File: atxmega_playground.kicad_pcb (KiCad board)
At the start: 2 copper layers, 87 parts, among them CON1 AVR-PDI-6, IC1 ATXMEGA32A4U-A, P1 USB_OTG, P2 CONN_01X02, P3 CONN_01X02, P4 CONN_01X08, P5 CONN_01X03, P6 CONN_01X04, P7 CONN_01X04, Q1 PMOS, Q2 NMOS, Q3 NMOS, Q4 NMOS, U1 NCP346, U10 WS2812B, U11 WS2812B, U12 74HC595_F, U13 74HC595_F, U14 AT25SF041, U15 LM75BD, U16 HIH9131, U2 LM3940, U3 ADM3315E, U4 HI-3110, U5 INA139, U6 WS2812B, U7 SN65220, U8 WS2812B, Y1 16MHz

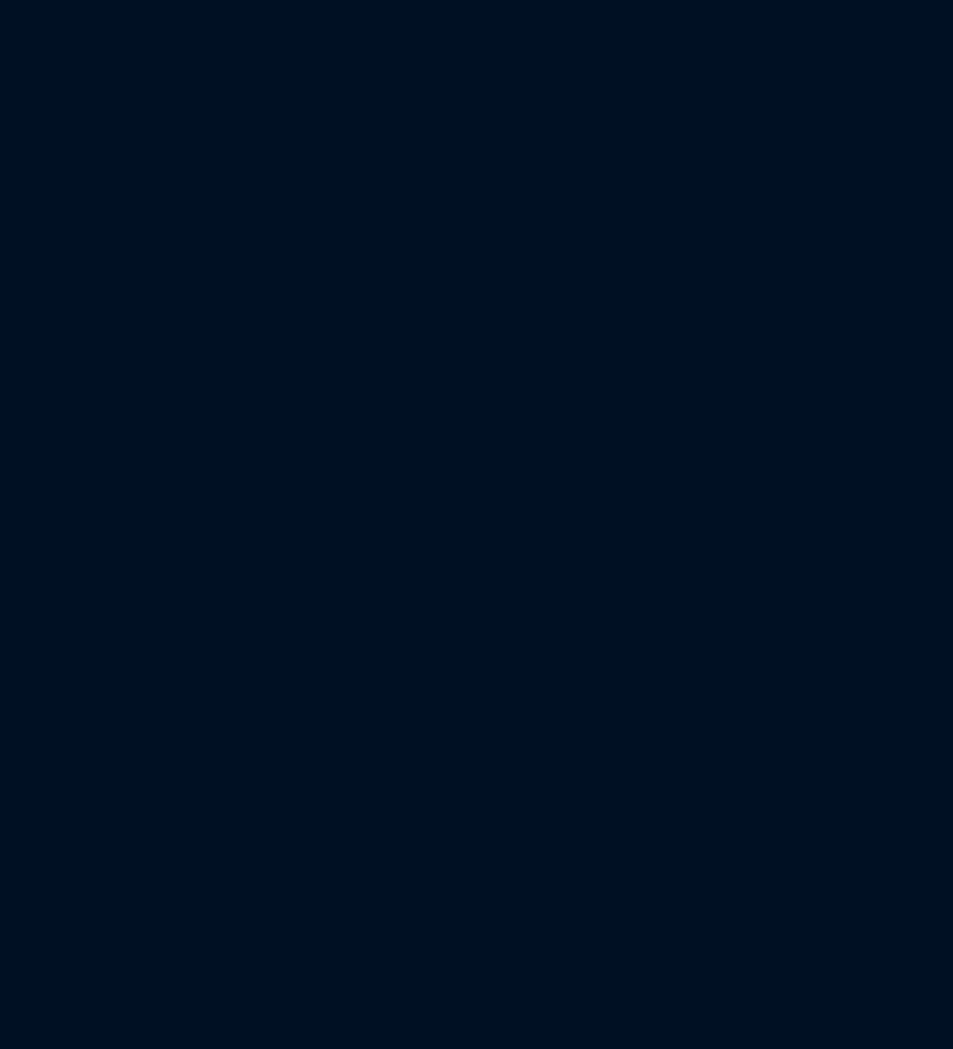
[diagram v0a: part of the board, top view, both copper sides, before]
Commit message: Add GPIO's ADC and 5V sensors, 7seg display footprint, and HIM's IMU's
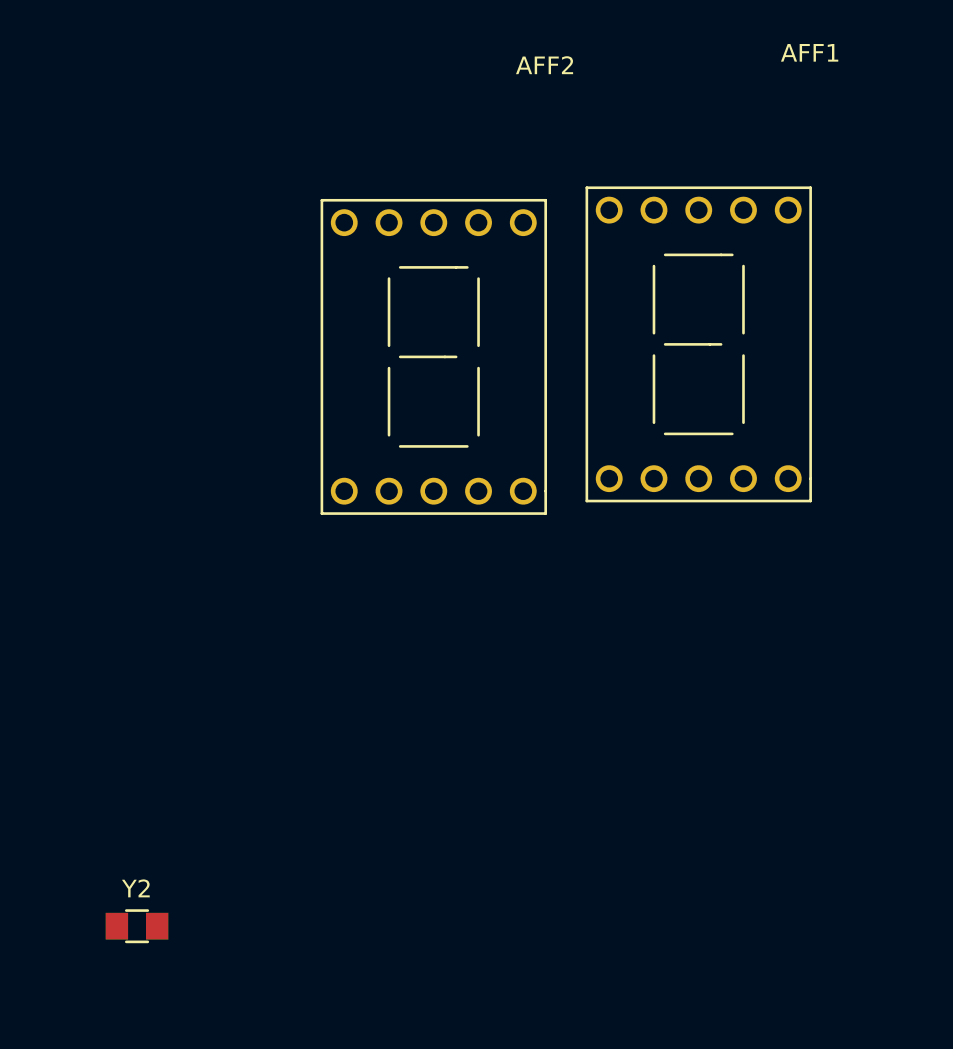
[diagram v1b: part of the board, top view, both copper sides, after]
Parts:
- added AFF1: 7SEGMENTS, atxmega:7seg_SC56-11SRWA, F.Cu at (201.0, 36.1)
- added AFF2: 7SEGMENTS, atxmega:7seg_SC56-11SRWA, F.Cu at (185.9, 36.8)
- added Y2: 32.768kHz, atxmega:R_0805, F.Cu at (174.2, 76.8)
- C15: value 0.1uF -> 10uF
- C16: value 0.22uF -> 0.1uF
- U15: value LM75BD -> REF195
- U16: value HIH9131 -> AD7708
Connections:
- net /ADC1 renamed /MC_ADC1
- net /ADC2 renamed /MC_ADC2
- net /ADC3 renamed /MC_ADC3
- net Net-(U16-Pad7) renamed /Vpressure
- C15 pad 1: Net-(C15-Pad1) -> +12V
- C16 pad 1: +3V3 -> +12V
- U15 pad 1: /SDA -> Net-(U15-Pad1)
- U15 pad 2: /SCL -> +12V
- U15 pad 3: Net-(U15-Pad3) -> +12V
- U15 pad 5: GND -> Net-(U15-Pad5)
- U15 pad 6: GND -> Net-(C17-Pad1)
- U15 pad 7: +3V3 -> Net-(U15-Pad7)
- U15 pad 8: +3V3 -> Net-(U15-Pad8)
- U16 pad 1: Net-(C15-Pad1) -> /ADC5
- U16 pad 2: GND -> /ADC6
- U16 pad 3: /SCL -> +5V
- U16 pad 4: /SDA -> GND
- U16 pad 5: Net-(U16-Pad5) -> GND
- U16 pad 6: Net-(U16-Pad6) -> Net-(C17-Pad1)
- U16 pad 8: +3V3 -> /Vtemp

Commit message: Basic layout, component positions mostly final
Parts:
- added C17: 1uF, atxmega:c_elec_18x21.5, F.Cu at (38.9, -26.9)
- added C18: 0.1uF, atxmega:C_0805, B.Cu at (118.0, 74.9)
- added C19: 10uF, atxmega:C_0805, F.Cu at (115.8, 79.2)
- added C20: 0.1uF, atxmega:C_0805, F.Cu at (117.9, 81.4)
- added C21: 0.1uF, atxmega:C_0805, B.Cu at (104.3, 79.9)
- added C22: 4pF, atxmega:C_0805, B.Cu at (109.3, 80.4)
- added C23: 4pF, atxmega:C_0805, B.Cu at (109.3, 84.5)
- added C24: 0.1uF, atxmega:C_0805, B.Cu at (124.5, 76.6)
- added C25: 0.1uF, atxmega:C_0805, B.Cu at (122.4, 81.4)
- added C26: 47pF, atxmega:C_0805, F.Cu at (115.7, 85.6)
- added C27: 0.1uF, atxmega:C_0805, B.Cu at (95.2, 56.5)
- added C28: 0.1uF, atxmega:C_0805, B.Cu at (91.9, 59.2)
- added C29: 0.1uF, atxmega:C_0805, B.Cu at (88.0, 59.2)
- added C30: 0.1uF, atxmega:C_0805, B.Cu at (82.3, 53.6)
- added C31: 2.2nF, atxmega:C_0805, B.Cu at (83.2, 58.4)
- added D6: D_Schottky, atxmega:R_0805, F.Cu at (140.3, 85.7)
- added IMU1: KMX62-1031, atxmega:KXG03_footprint, F.Cu at (91.8, 55.8)
- added IMU2: KXG03, atxmega:KXG03_footprint, F.Cu at (86.5, 55.9)
- added P8: CONN_01X07, Pin_Headers:Pin_Header_Straight_1x07_Pitch2.54mm, F.Cu at (130.0, 148.6)
- added R35: 51k, atxmega:R_0805, F.Cu at (117.7, 86.5)
- added TP3: 5V Input, atxmega:TESTPOINT, F.Cu at (132.6, 78.0)
- added TP4: TEST, atxmega:TESTPOINT, F.Cu at (134.2, 69.6)
- added TP5: TEST, atxmega:TESTPOINT, F.Cu at (132.6, 74.5)
- added U17: MPXH6101A, atxmega:SOIC-8_7.5x7.5mm_Pitch1.27mm, F.Cu at (124.7, 83.8)
- added U18: LM35, Housings_SOIC:SOIC-8_3.9x4.9mm_Pitch1.27mm, F.Cu at (124.0, 76.2)
- C11, C12, C13, C3, C4, C5, C6, C8, R13, R14, R15, R16, R17, R18, R19, R20, R21, R22, R23, R24, R25, R26, R27, R28, R3, R4, R5, R6, Y2: moved to B.Cu
- P4: value CONN_01X08 -> CONN_01X06
- Q1, Q2, Q3, Q4: footprint atxmega:SOT-23-5 -> atxmega:SOT-23-3_Handsoldering
- U15: footprint atxmega:TSSOP-8_4.4x3mm_Pitch0.65mm -> Housings_SOIC:SOIC-8_3.9x4.9mm_Pitch1.27mm
- U16: footprint Housings_SOIC:SOIC-8_3.9x4.9mm_Pitch1.27mm -> Housings_SOIC:SOIC-28W_7.5x17.9mm_Pitch1.27mm
- moved P5 202.2 mm to (81.3, 50.3), turned to 90 degrees
- moved S1 189.4 mm to (82.5, 62.7)
- moved R13 158.3 mm to (111.8, 53.8), turned to 270 degrees
- moved R14 157.5 mm to (111.8, 42.4), turned to 270 degrees
- moved P3 151.7 mm to (91.9, 88.0), turned to 270 degrees
- moved P7 150.5 mm to (109.2, 136.7), turned to 90 degrees
- moved D10 144.9 mm to (83.6, 43.2)
- moved D11 144.6 mm to (85.3, 45.2)
- moved D12 144.4 mm to (86.9, 47.2)
- moved U13 142.9 mm to (114.6, 55.1), turned to 180 degrees
- moved R29 141.0 mm to (87.9, 43.2), turned to 180 degrees
- moved R30 140.8 mm to (89.7, 45.2), turned to 180 degrees
- moved R31 140.7 mm to (91.2, 47.2), turned to 180 degrees
- moved D2 127.6 mm to (83.1, 74.2), turned to 270 degrees
- moved D1 127.0 mm to (83.1, 78.2), turned to 270 degrees
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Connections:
- AFF1 pad 5: Net-(AFF1-Pad5) -> (no net)
- AFF2 pad 5: Net-(AFF2-Pad5) -> (no net)
- CON1 pad 3: Net-(CON1-Pad3) -> (no net)
- CON1 pad 4: Net-(CON1-Pad4) -> (no net)
- IC1 pad 1: /LED2 -> /LED1
- IC1 pad 2: /LED3 -> /LED2
- IC1 pad 20: /PD_1 -> /~FLASH_CS
- IC1 pad 21: /PD_2 -> /~ADC_CS
- IC1 pad 24: /GPIO6 -> /IMU_INT1
- IC1 pad 25: /GPIO7 -> /IMU_INT2
- IC1 pad 29: /GPIO2 -> /SR_SER
- IC1 pad 3: /LED_DIN_3.3V -> (no net)
- IC1 pad 32: /GPIO3 -> /SR_RCLK
- IC1 pad 33: /GPIO4 -> /SR_SRCLK
- IC1 pad 4: /~FLASH_CS -> /LED3
- IC1 pad 40: /CURR_SENSE -> (no net)
- IC1 pad 44: /LED1 -> /CURR_SENSE
- IC1 pad 5: /SR_RCLK -> (no net)
- IC1 pad 6: /SR_RSCLK -> (no net)
- IC1 pad 7: /SR_SER -> (no net)
- P1 pad 1: Net-(P1-Pad1) -> (no net)
- P1 pad 4: Net-(P1-Pad4) -> (no net)
- P4 pad 2: /GPIO2 -> (no net)
- P4 pad 3: /GPIO3 -> (no net)
- P4 pad 4: /GPIO4 -> (no net)
- P4 pad 6: /GPIO6 -> GND
- P4 pad 7: /GPIO7 -> (no net)
- P4 pad 8: GND -> (no net)
- Q2 pad 2: /PD_1 -> (no net)
- Q3 pad 2: /PD_2 -> (no net)
- U11 pad 2: Net-(U11-Pad2) -> (no net)
- U12 pad 7: Net-(U12-Pad7) -> (no net)
- U12 pad 9: Net-(U12-Pad9) -> (no net)
- U13 pad 7: Net-(U13-Pad7) -> (no net)
- U14 pad 3: Net-(U14-Pad3) -> (no net)
- U14 pad 7: Net-(U14-Pad7) -> (no net)
- U15 pad 1: Net-(U15-Pad1) -> (no net)
- U15 pad 5: Net-(U15-Pad5) -> (no net)
- U15 pad 7: Net-(U15-Pad7) -> (no net)
- U15 pad 8: Net-(U15-Pad8) -> (no net)
- U16 pad 1: /ADC5 -> /Vpressure
- U16 pad 7: /Vpressure -> /ADC5
- U3 pad 11: Net-(U3-Pad11) -> (no net)
- U3 pad 12: Net-(U3-Pad12) -> (no net)
- U3 pad 13: Net-(U3-Pad13) -> (no net)
- U3 pad 14: Net-(U3-Pad14) -> (no net)
- U3 pad 16: Net-(U3-Pad16) -> (no net)
- U3 pad 17: Net-(U3-Pad17) -> (no net)
- U3 pad 8: Net-(U3-Pad8) -> (no net)
- U3 pad 9: Net-(U3-Pad9) -> (no net)
- U4 pad 12: Net-(U4-Pad12) -> (no net)
- U4 pad 17: Net-(U4-Pad17) -> (no net)
- U4 pad 18: /CAN_INT -> (no net)
- U4 pad 2: Net-(U4-Pad2) -> (no net)
- U4 pad 3: Net-(U4-Pad3) -> (no net)
- U4 pad 7: Net-(U4-Pad7) -> (no net)
- U6 pad 4: /LED_DIN_5V -> (no net)
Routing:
- net +5V: track 0.00 -> 185.1 mm, vias 0 -> 1
- net GND: track 0.00 -> 79.6 mm, vias 0 -> 33
- net /SPIC_MOSI: track 0.00 -> 43.6 mm, vias 0 -> 2
- net /SPIC_SCK: track 0.00 -> 42.0 mm, vias 0 -> 2
- net Net-(R15-Pad2): track 0.00 -> 38.6 mm, vias 0 -> 3
- net /SPIC_MISO: track 0.00 -> 37.8 mm, vias 0 -> 4
- net +3V3: track 0.00 -> 35.0 mm, vias 0 -> 11
- net Net-(R16-Pad2): track 0.00 -> 29.3 mm, vias 0 -> 1
- net Net-(R17-Pad2): track 0.00 -> 29.1 mm, vias 0 -> 1
- net Net-(R18-Pad2): track 0.00 -> 27.0 mm, vias 0 -> 1
- net Net-(R22-Pad2): track 0.00 -> 26.6 mm, vias 0 -> 1
- net /~CAN_CS: track 0.00 -> 25.3 mm
- net Net-(R20-Pad2): track 0.00 -> 24.4 mm, vias 0 -> 1
- net Net-(R19-Pad2): track 0.00 -> 23.8 mm, vias 0 -> 1
- net Net-(R23-Pad2): track 0.00 -> 23.8 mm, vias 0 -> 1
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- added copper zone on F.Cu, net +3V3
- added copper zone on B.Cu, net GND
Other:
- board outline added: 101.3 x 96.5 mm
- net class Default: via_drill 0.4 -> 0.3048
- rule pad_to_mask_clearance: 0.2 -> 0.0762
